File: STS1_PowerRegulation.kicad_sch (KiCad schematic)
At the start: 21 parts, among them Q8 BSL307SP, U24 MCP1725-3302E_MC, U3 MCP1725-3302E_MC

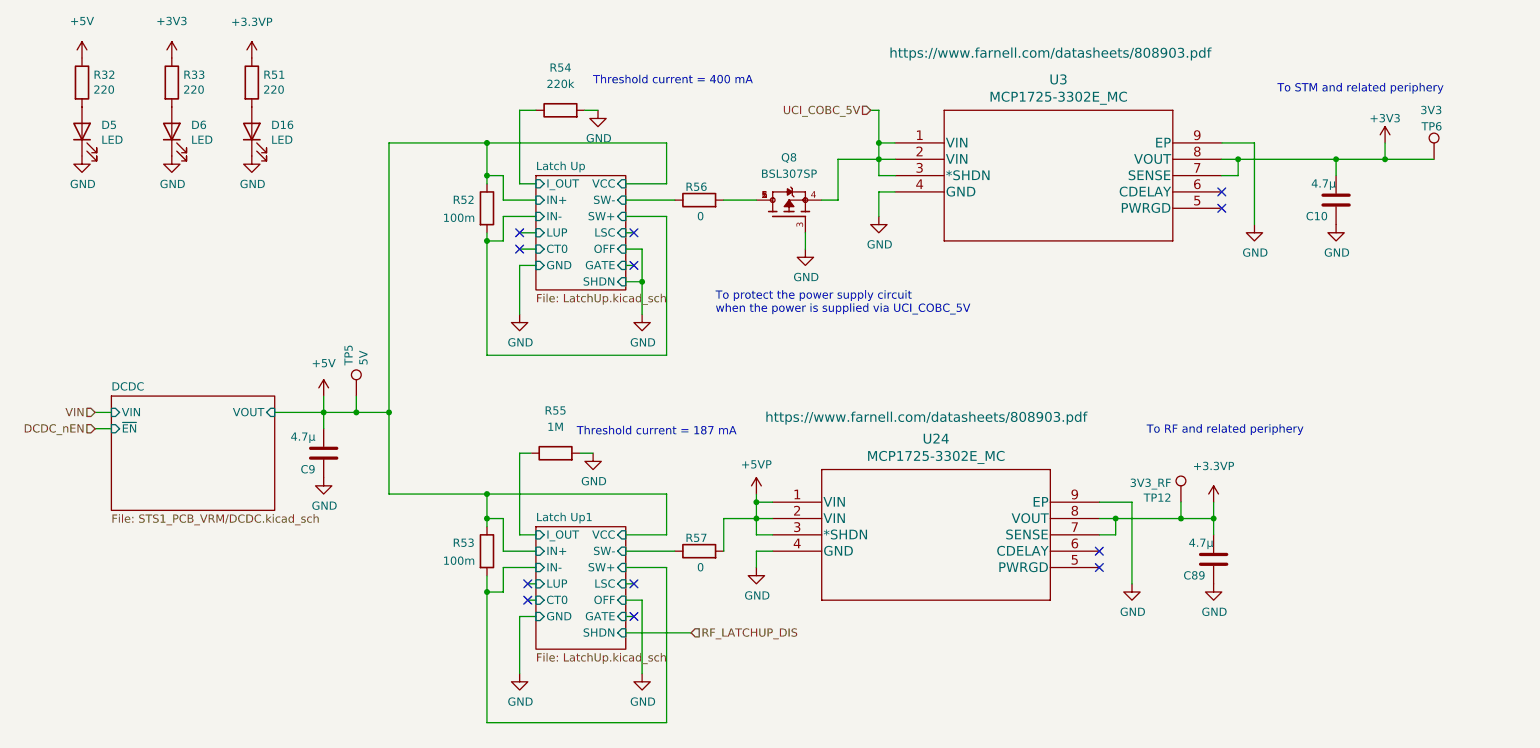
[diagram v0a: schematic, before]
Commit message: Add manufacture number and JLCPCB part number to components
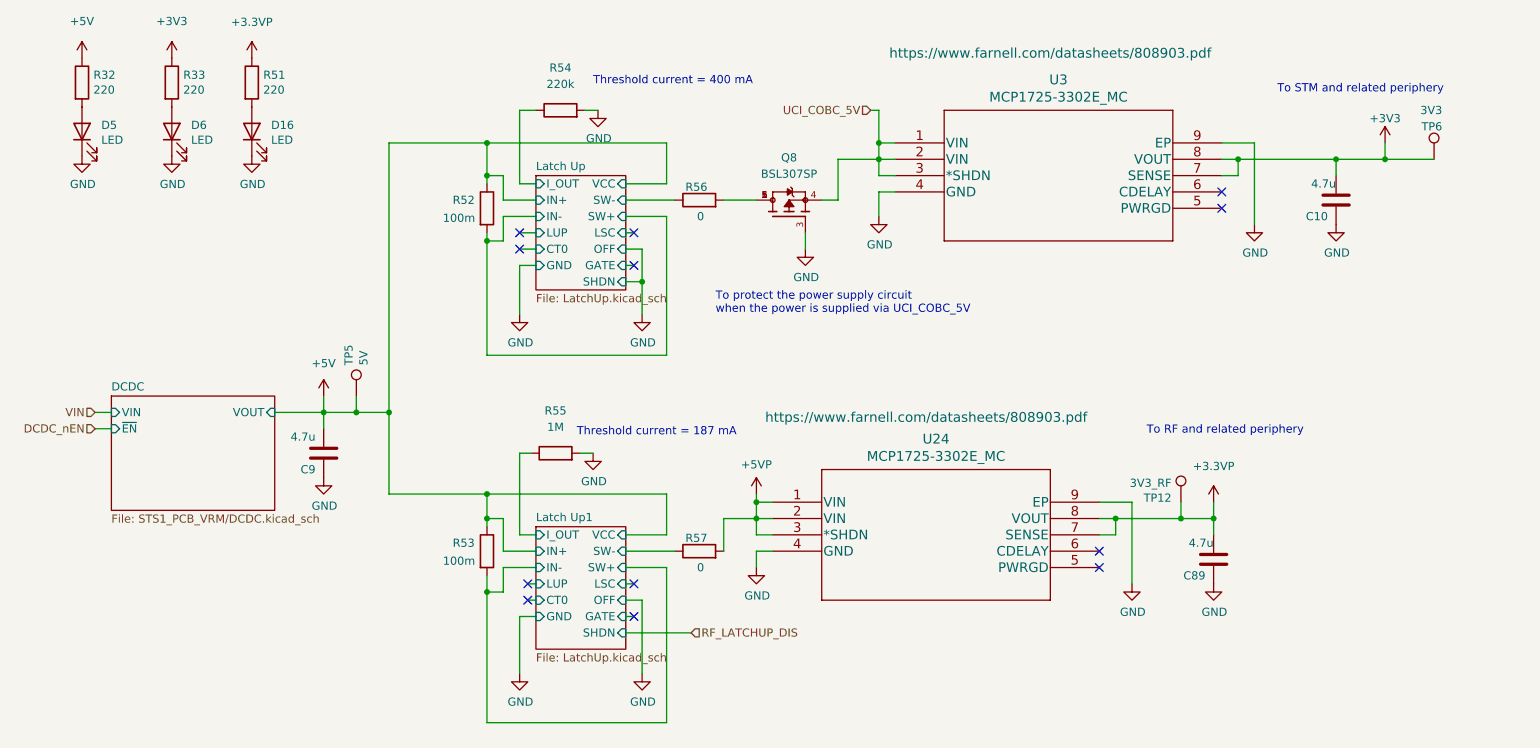
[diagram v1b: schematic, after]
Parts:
- C10, C89, C9: value 4.7µ -> 4.7u; JLCPCB Part # (none) -> C5969198; Manufacturer_Part_Number (none) -> CL10A475KP8NNWC
- D16, D5, D6: Manufacturer_Part_Number (none) -> 598-8160-107F
- Q8: JLCPCB Part # (none) -> C534457; Manufacturer_Part_Number (none) -> BSL307SP H6327
- R32, R33, R51: JLCPCB Part # (none) -> C4257599; Manufacturer_Part_Number (none) -> ERJ-H3EF2200V
- R52, R53: JLCPCB Part # (none) -> C1698656; Manufacturer_Part_Number (none) -> RCWL0603R100JQEA
- R54: JLCPCB Part # (none) -> C4285297; Manufacturer_Part_Number (none) -> ERJ-H3EF5102V
- R55: Manufacturer_Part_Number (none) -> MR06X1004FTL
- R56, R57: JLCPCB Part # (none) -> C4117710; Manufacturer_Part_Number (none) -> ERJ-H3G0R00V
- U24, U3: JLCPCB Part # (none) -> C635002; Manufacturer_Part_Number (none) -> MCP1725-3302E/MC
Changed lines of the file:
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@@
       (effects (font (size 1.524 1.524)))
+    )
+    (property "Manufacturer_Part_Number" "MCP1725-3302E/MC " (id 4) (at 158.75 38.1 0)
+      (effects (font (size 1.27 1.27)) hide)
+    )
+    (property "JLCPCB Part #" "C635002" (id 5) (at 158.75 38.1 0)
+      (effects (font (size 1.27 1.27)) hide)
     )
     (pin "1")
@@
       (effects (font (size 1.27 1.27)) (justify left))
     )
-    (property "Value" "4.7µ" (id 1) (at 68.58 83.82 0)
+    (property "Value" "4.7u" (id 1) (at 68.58 83.82 0)
       (effects (font (size 1.27 1.27)) (justify left))
     )
@@
     )
     (property "Datasheet" "~" (id 3) (at 69.85 86.36 0)
+      (effects (font (size 1.27 1.27)) hide)
+    )
+    (property "JLCPCB Part #" "C5969198" (id 4) (at 69.85 86.36 0)
+      (effects (font (size 1.27 1.27)) hide)
+    )
+    (property "Manufacturer_Part_Number" "CL10A475KP8NNWC " (id 5) (at 69.85 86.36 0)
       (effects (font (size 1.27 1.27)) hide)
     )
@@
       (effects (font (size 1.27 1.27)) (justify left))
     )
-    (property "Value" "4.7µ" (id 1) (at 227.33 44.45 0)
+    (property "Value" "4.7u" (id 1) (at 227.33 44.45 0)
       (effects (font (size 1.27 1.27)) (justify left))
     )
@@
     )
     (property "Datasheet" "~" (id 3) (at 227.33 46.99 0)
+      (effects (font (size 1.27 1.27)) hide)
+    )
+    (property "JLCPCB Part #" "C5969198" (id 4) (at 227.33 46.99 0)
+      (effects (font (size 1.27 1.27)) hide)
+    )
+    (property "Manufacturer_Part_Number" "CL10A475KP8NNWC " (id 5) (at 227.33 46.99 0)
       (effects (font (size 1.27 1.27)) hide)
     )
@@
       (effects (font (size 1.27 1.27)) hide)
     )
+    (property "Manufacturer_Part_Number" "MR06X1004FTL " (id 4) (at 105.918 86.36 0)
+      (effects (font (size 1.27 1.27)) hide)
+    )
     (pin "1")
     (pin "2")
@@
       (effects (font (size 1.27 1.27)) hide)
     )
+    (property "Manufacturer_Part_Number" "598-8160-107F " (id 4) (at 58.674 36.322 90)
+      (effects (font (size 1.27 1.27)) hide)
+    )
+    (property "JLCPCB Part #" "" (id 5) (at 58.674 36.322 90)
+      (effects (font (size 1.27 1.27)) hide)
+    )
     (pin "1")
     (pin "2")
@@
       (effects (font (size 1.27 1.27)) (justify left))
     )
-    (property "Value" "4.7µ" (id 1) (at 208.28 100.33 0)
+    (property "Value" "4.7u" (id 1) (at 208.28 100.33 0)
       (effects (font (size 1.27 1.27)) (justify left))
     )
@@
       (effects (font (size 1.27 1.27)) hide)
     )
+    (property "JLCPCB Part #" "C5969198" (id 4) (at 208.28 102.87 0)
+      (effects (font (size 1.27 1.27)) hide)
+    )
+    (property "Manufacturer_Part_Number" "CL10A475KP8NNWC " (id 5) (at 208.28 102.87 0)
+      (effects (font (size 1.27 1.27)) hide)
+    )
     (pin "1")
     (pin "2")
@@
     )
     (property "Datasheet" "~" (id 3) (at 46.228 28.702 0)
+      (effects (font (size 1.27 1.27)) hide)
+    )
+    (property "JLCPCB Part #" "C4257599" (id 4) (at 46.228 28.702 0)
+      (effects (font (size 1.27 1.27)) hide)
+    )
+    (property "Manufacturer_Part_Number" "ERJ-H3EF2200V" (id 5) (at 46.228 28.702 0)
       (effects (font (size 1.27 1.27)) hide)
     )
@@
       (effects (font (size 1.27 1.27)) hide)
     )
+    (property "Manufacturer_Part_Number" "598-8160-107F " (id 4) (at 32.258 36.322 90)
+      (effects (font (size 1.27 1.27)) hide)
+    )
+    (property "JLCPCB Part #" "" (id 5) (at 32.258 36.322 90)
+      (effects (font (size 1.27 1.27)) hide)
+    )
     (pin "1")
     (pin "2")
@@
     )
     (property "Datasheet" "~" (id 3) (at 128.27 46.99 0)
+      (effects (font (size 1.27 1.27)) hide)
+    )
+    (property "JLCPCB Part #" "C4117710" (id 4) (at 128.27 46.99 0)
+      (effects (font (size 1.27 1.27)) hide)
+    )
+    (property "Manufacturer_Part_Number" "ERJ-H3G0R00V" (id 5) (at 128.27 46.99 0)
       (effects (font (size 1.27 1.27)) hide)
     )
@@
       (effects (font (size 1.27 1.27)) (justify bottom) hide)
     )
-    (property "Description" "\nP-Channel 30 V 5.5A (Ta) 2W (Ta) Surface Mount PG-TSOP-6-1\n" (id 5) (at 142.24 49.53 0)
+    (property "Description" "P-Channel 30 V 5.5A (Ta) 2W (Ta) Surface Mount PG-TSOP-6-1" (id 5) (at 142.24 49.53 0)
       (effects (font (size 1.27 1.27)) (justify bottom) hide)
     )
@@
     (property "Check_prices" "https://www.snapeda.com/parts/BSL307SP/Infineon+Technologies/view-part/?ref=eda" (id 12) (at 125.73 49.53 0)
       (effects (font (size 1.27 1.27)) (justify bottom) hide)
+    )
+    (property "Manufacturer_Part_Number" "BSL307SP H6327" (id 13) (at 142.24 49.53 90)
+      (effects (font (size 1.27 1.27)) hide)
+    )
+    (property "JLCPCB Part #" "C534457" (id 14) (at 142.24 49.53 90)
+      (effects (font (size 1.27 1.27)) hide)
     )
     (pin "1")
@@
       (effects (font (size 1.27 1.27)) hide)
     )
+    (property "JLCPCB Part #" "C1698656" (id 4) (at 95.25 48.26 0)
+      (effects (font (size 1.27 1.27)) hide)
+    )
+    (property "Manufacturer_Part_Number" "RCWL0603R100JQEA " (id 5) (at 95.25 48.26 0)
+      (effects (font (size 1.27 1.27)) hide)
+    )
     (pin "1")
     (pin "2")
@@
       (effects (font (size 1.27 1.27)) hide)
     )
+    (property "JLCPCB Part #" "C4117710" (id 4) (at 128.27 101.6 0)
+      (effects (font (size 1.27 1.27)) hide)
+    )
+    (property "Manufacturer_Part_Number" "ERJ-H3G0R00V" (id 5) (at 128.27 101.6 0)
+      (effects (font (size 1.27 1.27)) hide)
+    )
     (pin "1")
     (pin "2")
@@
       (effects (font (size 1.27 1.27)) hide)
     )
+    (property "JLCPCB Part #" "C1698656" (id 4) (at 95.25 101.6 0)
+      (effects (font (size 1.27 1.27)) hide)
+    )
+    (property "Manufacturer_Part_Number" "RCWL0603R100JQEA " (id 5) (at 95.25 101.6 0)
+      (effects (font (size 1.27 1.27)) hide)
+    )
     (pin "1")
     (pin "2")
@@
     (property "Datasheet" "https://www.farnell.com/datasheets/808903.pdf" (id 3) (at 163.576 80.772 0)
       (effects (font (size 1.524 1.524)))
+    )
+    (property "Manufacturer_Part_Number" "MCP1725-3302E/MC" (id 4) (at 139.7 93.98 0)
+      (effects (font (size 1.27 1.27)) hide)
+    )
+    (property "JLCPCB Part #" "C635002" (id 5) (at 139.7 93.98 0)
+      (effects (font (size 1.27 1.27)) hide)
     )
     (pin "1")
@@
       (effects (font (size 1.27 1.27)) hide)
     )
+    (property "JLCPCB Part #" "C4285297" (id 4) (at 106.68 33.02 0)
+      (effects (font (size 1.27 1.27)) hide)
+    )
+    (property "Manufacturer_Part_Number" "ERJ-H3EF5102V" (id 5) (at 106.68 33.02 0)
+      (effects (font (size 1.27 1.27)) hide)
+    )
     (pin "1")
     (pin "2")
@@
       (effects (font (size 1.27 1.27)) hide)
     )
+    (property "JLCPCB Part #" "C4257599" (id 4) (at 58.674 28.702 0)
+      (effects (font (size 1.27 1.27)) hide)
+    )
+    (property "Manufacturer_Part_Number" "ERJ-H3EF2200V" (id 5) (at 58.674 28.702 0)
+      (effects (font (size 1.27 1.27)) hide)
+    )
     (pin "1")
     (pin "2")
@@
       (effects (font (size 1.27 1.27)) hide)
     )
+    (property "Manufacturer_Part_Number" "598-8160-107F " (id 4) (at 46.228 36.322 90)
+      (effects (font (size 1.27 1.27)) hide)
+    )
+    (property "JLCPCB Part #" "" (id 5) (at 46.228 36.322 90)
+      (effects (font (size 1.27 1.27)) hide)
+    )
     (pin "1")
     (pin "2")
@@
       (effects (font (size 1.27 1.27)) hide)
     )
+    (property "JLCPCB Part #" "C4257599" (id 4) (at 32.258 28.702 0)
+      (effects (font (size 1.27 1.27)) hide)
+    )
+    (property "Manufacturer_Part_Number" "ERJ-H3EF2200V" (id 5) (at 32.258 28.702 0)
+      (effects (font (size 1.27 1.27)) hide)
+    )

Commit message: Exclude testpoints from bill of materials
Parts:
- TP12, TP6: now left out of the parts list
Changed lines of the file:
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@@
   )
   (symbol (lib_id "Connector:TestPoint") (at 242.57 40.64 0) (unit 1)
-    (in_bom yes) (on_board yes)
+    (in_bom no) (on_board yes)
     (property "Reference" "TP6" (id 0) (at 243.84 35.56 0)
       (effects (font (size 1.27 1.27)) (justify right))
@@
   )
   (symbol (lib_id "Connector:TestPoint") (at 203.2 93.98 0) (unit 1)
-    (in_bom yes) (on_board yes)
+    (in_bom no) (on_board yes)
     (property "Reference" "TP12" (id 0) (at 201.7268 93.3196 0)
       (effects (font (size 1.27 1.27)) (justify right))

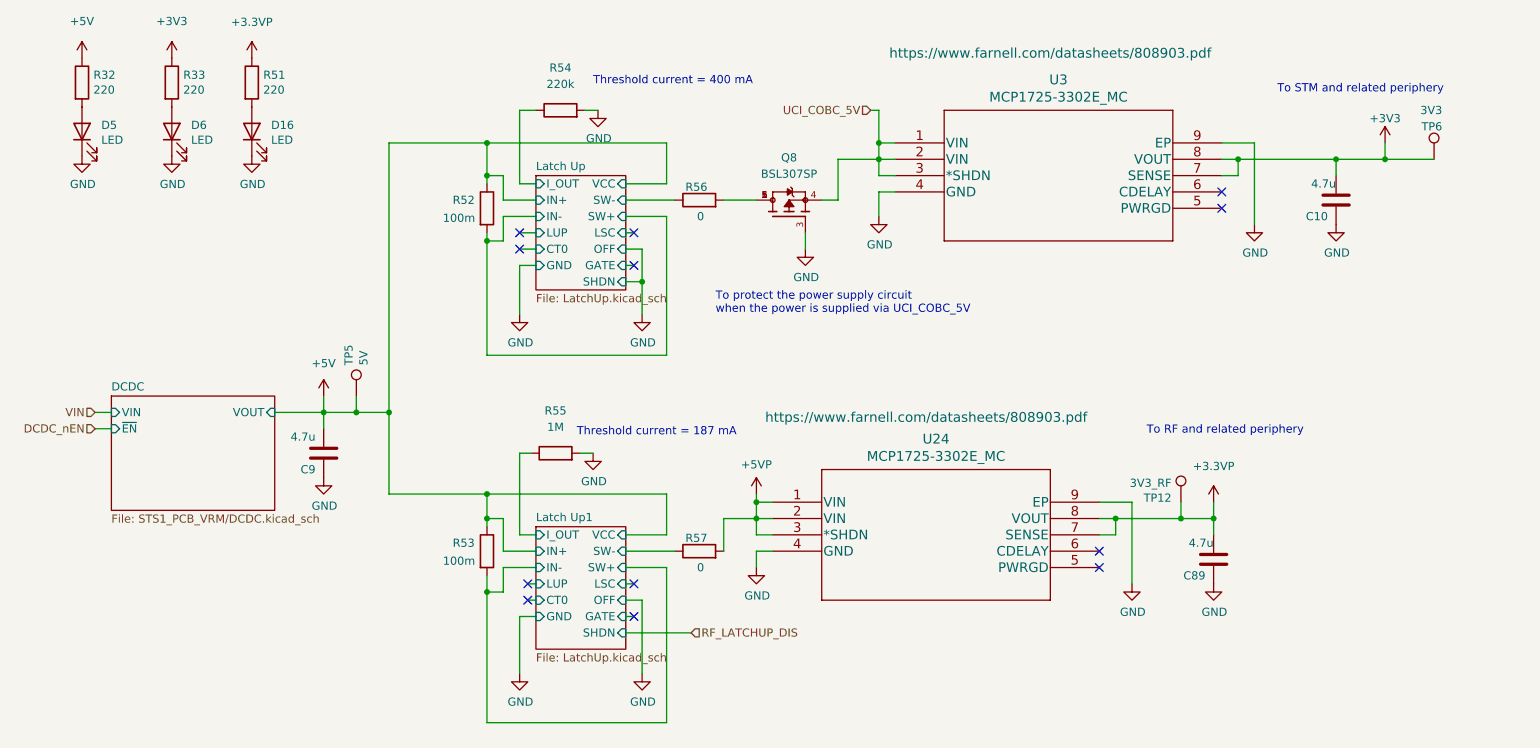
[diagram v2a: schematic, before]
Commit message: Remove Q8 and add zener diodes to protect output of LDOs and latch-up protection circuits
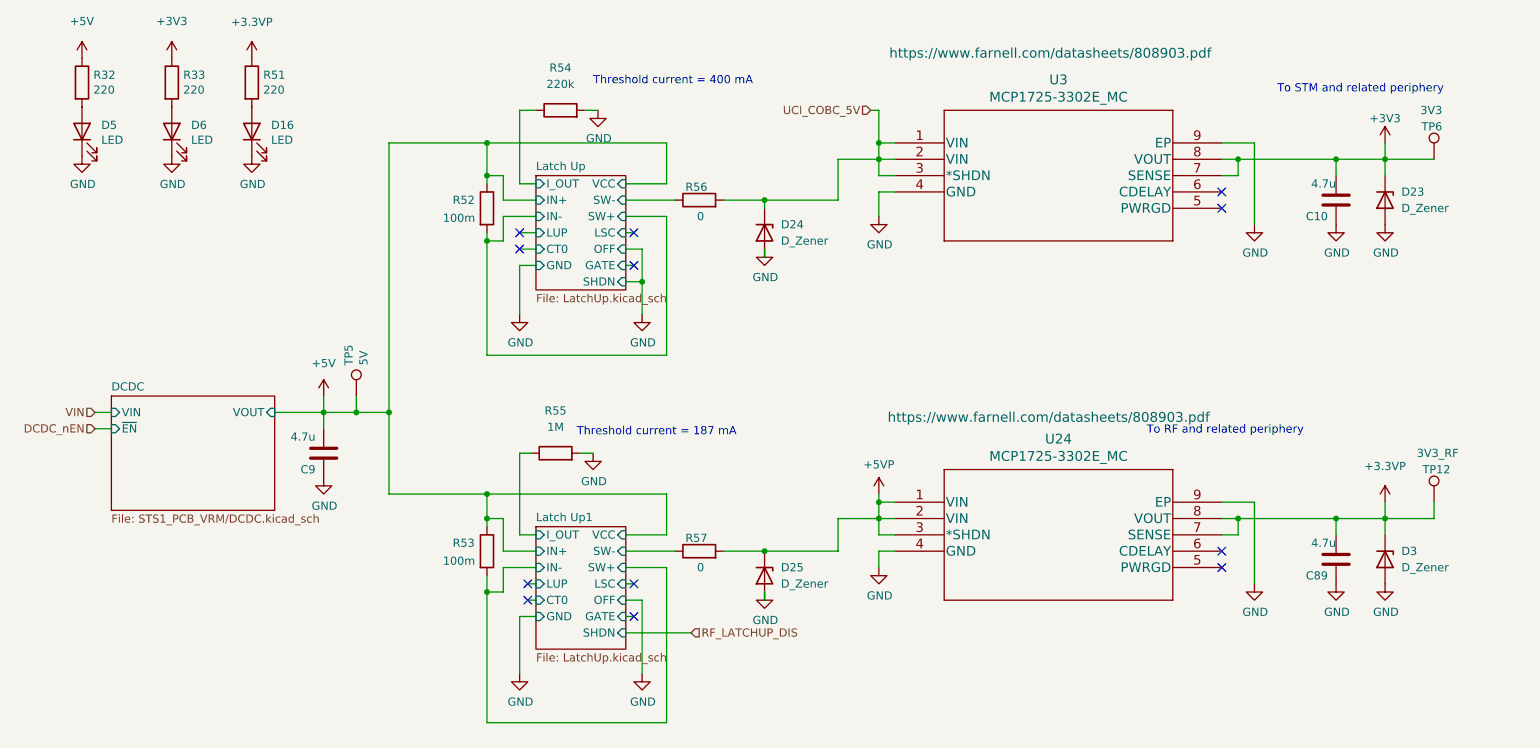
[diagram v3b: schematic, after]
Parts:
- removed Q8: BSL307SP, Package_SO:TSOP-6_1.65x3.05mm_P0.95mm, symbol STS1_COBC_V2-rescue:BSL307SP
- added D23, D24, D25, D3: D_Zener, Diode_SMD:D_SOD-123, symbol Device:D_Zener
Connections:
- net +3.3VP: now also D3.1 (K)
- net +3V3: now also D23.1 (K)
- net +5VP: now also D25.1 (K)
- net GND: now also D23.2 (A), D24.2 (A), D25.2 (A), D3.2 (A)
- net UCI_COBC_5V: now also R56.2, D24.1 (K)
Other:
- note removed: "To protect the power supply circuit when the power is supplied via UCI_COBC_5V"
- moved on the sheet: C89, TP12, U24
